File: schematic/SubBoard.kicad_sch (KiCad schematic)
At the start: 0 parts

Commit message: Progress on KiCAD schematics
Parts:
- added DS1: LCM SLOT, Display:WC1602A, symbol Display_Character:WC1602A
- added J2: LCM SLOT CONNECTOR, symbol Connector_Generic:Conn_02x11_Odd_Even
- added SD1: SD CARD SLOT, symbol Connector:Micro_SD_Card_Det2
- added SD2: SD CARD SLOT CONNECTOR, symbol Connector_Generic:Conn_02x08_Odd_Even
- added SW1: UP, Button_Switch_THT:SW_PUSH_6mm, symbol PCM_SL_Devices:Push_Button
- added SW2: DOWN, Button_Switch_THT:SW_PUSH_6mm, symbol PCM_SL_Devices:Push_Button
- added SW3: RIGHT, Button_Switch_THT:SW_PUSH_6mm, symbol PCM_SL_Devices:Push_Button
- added SW4: LEFT, Button_Switch_THT:SW_PUSH_6mm, symbol PCM_SL_Devices:Push_Button
- added SW5: ENTER, Button_Switch_THT:SW_PUSH_6mm, symbol PCM_SL_Devices:Push_Button
- added SW6: ESCAPE, Button_Switch_THT:SW_PUSH_6mm, symbol PCM_SL_Devices:Push_Button
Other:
- title: (none) -> Da Vinci Jr. 1.0 Sub Board schematic

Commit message: Update sub-board schematic
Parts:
- added Q2: FMBT3904W, Package_TO_SOT_SMD:SOT-323_SC-70, symbol Transistor_BJT:2SC4213
- added R1, R11, R21, R23, R25, R8: 100k, Resistor_THT:R_Axial_DIN0207_L6.3mm_D2.5mm_P10.16mm_Horizontal, symbol PCM_SL_Resistors:100k
- added R29: 2ohm, Resistor_THT:R_Axial_DIN0207_L6.3mm_D2.5mm_P10.16mm_Horizontal, symbol PCM_SL_Resistors:2ohm
- added R3, R30: 1k, Resistor_THT:R_Axial_DIN0207_L6.3mm_D2.5mm_P10.16mm_Horizontal, symbol PCM_SL_Resistors:1k
- added R5: 10k, Resistor_THT:R_Axial_DIN0207_L6.3mm_D2.5mm_P10.16mm_Horizontal, symbol PCM_SL_Resistors:10k
- added U1, U2: TXB0108PW, Package_SO:TSSOP-20_4.4x6.5mm_P0.65mm, symbol Logic_LevelTranslator:TXB0108PW
- renumbered DS1 to J3
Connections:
- net at SD1.1 (DAT2): now also SD2.16 (Pin_16)
- net at SD1.2 (DAT3/CD): now also SD2.14 (Pin_14)
- net at SD1.3 (CMD): now also SD2.12 (Pin_12)
- net at SD1.4 (VDD): now also SD2.9 (Pin_9)
- net at SD1.5 (CLK): now also SD2.7 (Pin_7)
- net GNDREF: now reaches SD1.6 (VSS)
- net GNDREF: now also J2.2 (Pin_2), J2.21 (Pin_21), J3.1 (VSS), SD1.SH (SHIELD), SD2.11 (Pin_11), SD2.13 (Pin_13), SD2.15 (Pin_15), SD2.2 (Pin_2), SD2.4 (Pin_4), SD2.6 (Pin_6), SW1.1, SW2.2, SW3.2, SW4.2, SW5.2, SW6.2, Q2.2 (E), R3.1
- net at SD1.7 (DAT0): now also SD2.5 (Pin_5)
- net at SD1.8 (DAT1): now also SD2.3 (Pin_3)
- net at SD1.9 (DET_B): now also SD2.10 (Pin_10)
- net at SW6.1: now also J2.15 (Pin_15), R25.1
- net at SW2.1: now also J2.16 (Pin_16), R8.1
- net at SW3.1: now also J2.19 (Pin_19), R11.1
- net at SW1.2: now also J2.18 (Pin_18), R1.1
- net at SW4.1: now also J2.17 (Pin_17), R21.1
- net at J2.1 (Pin_1): now also J3.2 (VDD), R29.2, R5.1, U1.19 (V_{CCB})
- net at J2.14 (Pin_14): now also R30.1
- net at J2.20 (Pin_20): now also SW5.1, R23.1
- net +5V: now reaches J2.22 (Pin_22)
- net +5V: now also R1.2, R11.2, R21.2, R23.2, R25.2, R8.2
- net at J3.15 (LED(+)): now also R29.1
- net at J3.16 (LED(-)): now also Q2.3 (C)
- net at J3.3 (VO): now also R3.2, R5.2
- new net: Q2.1 (B), R30.2
- no-connect marks 0 -> 3
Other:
- moved on the sheet: SW1, SW2

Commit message: Complete SubBoard schematic tracing
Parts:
- added R2, R28: 1k, Resistor_THT:R_Axial_DIN0207_L6.3mm_D2.5mm_P10.16mm_Horizontal, symbol PCM_SL_Resistors:1k
- R29: value 2ohm -> 2.7ohm
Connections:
- net GNDREF: now also U1.11 (GND), U2.11 (GND)
- net at J2.1 (Pin_1), J3.2 (VDD), R29.2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: now also U2.19 (V_{CCB})
- net +3.3V: now reaches SD1.4 (VDD), SD2.9 (Pin_9)
- net +3.3V: now also U1.2 (V_{CCA}), U2.2 (V_{CCA}), R2.2, R28.2
- net at U1.10 (OE): now also J3.14 (D7), U2.10 (OE), U2.12 (B8), R2.1, R28.1
- net at U1.15 (B5): now also J3.4 (RS)
- net at U1.16 (B4): now also J3.5 (R/W)
- net at U1.17 (B3): now also J3.6 (E)
- net at U1.4 (A3): now also J2.3 (Pin_3)
- net at U1.5 (A4): now also J2.4 (Pin_4)
- net at U1.6 (A5): now also J2.5 (Pin_5)
- net at J2.10 (Pin_10): now also U2.6 (A5)
- net at J2.11 (Pin_11): now also U2.7 (A6)
- net at J2.12 (Pin_12): now also U2.8 (A7)
- net at J2.13 (Pin_13): now also U2.9 (A8)
- net at J2.6 (Pin_6): now also U2.1 (A1)
- net at J2.7 (Pin_7): now also U2.3 (A2)
- net at J2.8 (Pin_8): now also U2.4 (A3)
- net at J2.9 (Pin_9): now also U2.5 (A4)
- net at J3.10 (D3): now also U2.16 (B4)
- net at J3.11 (D4): now also U2.15 (B5)
- net at J3.12 (D5): now also U2.14 (B6)
- net at J3.13 (D6): now also U2.13 (B7)
- net at J3.7 (D0): now also U2.20 (B1)
- net at J3.8 (D1): now also U2.18 (B2)
- net at J3.9 (D2): now also U2.17 (B3)
- no-connect marks 3 -> 13
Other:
- moved on the sheet: U2

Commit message: Update board schematics
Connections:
- net +3.3V: now also SD1.5 (VDD); no longer SD1.4 (VDD)
- net GNDREF: now also SD1.4 (VSS1), SD1.7 (VSS2); no longer SD1.6 (VSS)
- net at SD2.7 (Pin_7): now also SD1.6 (CLK); no longer SD1.5 (CLK)
- net at SD2.5 (Pin_5): now also SD1.8 (DAT0); no longer SD1.7 (DAT0)
- net at SD2.3 (Pin_3): now also SD1.9 (DAT1); no longer SD1.8 (DAT1)
- net at SD2.10 (Pin_10): now also SD1.11 (CD); no longer SD1.9 (DET_B)
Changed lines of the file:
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@@
 		(comment 1 "KEY/LCM/SD")
 	)
-	(text_box "DET_A is WP (Write Protect), DET_B is CD (Card Detect)"
-		(exclude_from_sim no)
-		(at 135.89 38.1 0)
-		(size 16.51 15.24)
-		(margins 0.9525 0.9525 0.9525 0.9525)
-		(stroke
-			(width 0)
-			(type solid)
-		)
-		(fill
-			(type none)
-		)
-		(effects
-			(font
-				(size 1.27 1.27)
-			)
-			(justify left top)
-		)
-	)
 	(junction
 		(at 232.41 153.67)
@@
 	)
 	(junction
+		(at 148.59 80.01)
+		(diameter 0)
+		(color 0 0 0 0)
+	)
+	(junction
 		(at 246.38 121.92)
 		(diameter 0)
@@
 	(wire
 		(pts
-			(xy 148.59 74.93) (xy 148.59 111.76)
+			(xy 151.13 74.93) (xy 151.13 111.76)
 		)
 		(stroke
@@
 	(wire
 		(pts
+			(xy 148.59 80.01) (xy 163.83 80.01)
+		)
+		(stroke
+			(width 0)
+			(type default)
+		)
+	)
+	(wire
+		(pts
 			(xy 83.82 74.93) (xy 83.82 76.2)
 		)
@@
 	(wire
 		(pts
-			(xy 151.13 114.3) (xy 234.95 114.3)
+			(xy 153.67 114.3) (xy 234.95 114.3)
 		)
 		(stroke
@@
 	(wire
 		(pts
-			(xy 140.97 80.01) (xy 163.83 80.01)
+			(xy 140.97 80.01) (xy 148.59 80.01)
 		)
 		(stroke
@@
 	(wire
 		(pts
-			(xy 151.13 74.93) (xy 151.13 114.3)
+			(xy 153.67 74.93) (xy 153.67 114.3)
 		)
 		(stroke
@@
 	(wire
 		(pts
-			(xy 148.59 111.76) (xy 232.41 111.76)
+			(xy 151.13 111.76) (xy 232.41 111.76)
 		)
 		(stroke
@@
 	(wire
 		(pts
-			(xy 153.67 74.93) (xy 153.67 116.84)
+			(xy 156.21 74.93) (xy 156.21 116.84)
 		)
 		(stroke
@@
 	(wire
 		(pts
-			(xy 153.67 116.84) (xy 237.49 116.84)
+			(xy 156.21 116.84) (xy 237.49 116.84)
 		)
 		(stroke
@@
 	(wire
 		(pts
+			(xy 148.59 74.93) (xy 148.59 80.01)
+		)
+		(stroke
+			(width 0)
+			(type default)
+		)
+	)
+	(wire
+		(pts
 			(xy 209.55 129.54) (xy 215.9 129.54)
 		)
@@
 	(wire
 		(pts
-			(xy 130.81 31.75) (xy 130.81 27.94)
+			(xy 132.08 31.75) (xy 132.08 27.94)
 		)
 		(stroke
@@
 	(wire
 		(pts
-			(xy 130.81 27.94) (xy 123.19 27.94)
+			(xy 132.08 27.94) (xy 123.19 27.94)
 		)
 		(stroke
@@
 	(symbol
 		(lib_id "Connector:Micro_SD_Card_Det2")
-		(at 143.51 52.07 270)
+		(at 144.78 52.07 270)
 		(mirror x)
 		(unit 1)
@@
 		(dnp no)
 		(property "Reference" "SD1"
-			(at 125.73 50.1649 90)
+			(at 127 50.1649 90)
 			(show_name no)
 			(do_not_autoplace no)
@@
 		)
 		(property "Value" "SD CARD SLOT"
-			(at 125.73 52.7049 90)
+			(at 127 52.7049 90)
 			(show_name no)
 			(do_not_autoplace no)
@@
 		)
 		(property "Footprint" ""
-			(at 161.29 0 0)
+			(at 162.56 0 0)
 			(hide yes)
 			(show_name no)
@@
 		)
 		(property "Datasheet" "https://www.hirose.com/en/product/document?clcode=&productname=&series=DM3&documenttype=Catalog&lang=en&documentid=D49662_en"
-			(at 146.05 49.53 0)
+			(at 147.32 49.53 0)
 			(hide yes)
 			(show_name no)
@@
 		)
 		(property "Description" "Micro SD Card Socket with two card detection pins"
-			(at 143.51 52.07 0)
+			(at 144.78 52.07 0)
 			(hide yes)
 			(show_name no)
@@
 		(pin "10"
 		)
+		(pin "11"
+		)
 		(instances

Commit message: Organize hardware documentation and pinouts
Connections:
- net +3.3V: now also SD2.8 (Pin_8)
- no-connect marks 13 -> 12
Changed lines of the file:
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@@
+		(color 0 0 0 0)
+	)
+	(junction
+		(at 213.36 156.21)
+		(diameter 0)
 		(color 0 0 0 0)
 	)
@@
 	)
 	(no_connect
-		(at 227.33 138.43)
-	)
-	(no_connect
 		(at 52.07 111.76)
 	)
@@
 	(wire
 		(pts
+			(xy 227.33 138.43) (xy 227.33 137.16)
+		)
+		(stroke
+			(width 0)
+			(type default)
+		)
+	)
+	(wire
+		(pts
 			(xy 52.07 104.14) (xy 67.31 104.14)
 		)
@@
 	(wire
 		(pts
+			(xy 213.36 137.16) (xy 213.36 156.21)
+		)
+		(stroke
+			(width 0)
+			(type default)
+		)
+	)
+	(wire
+		(pts
 			(xy 90.17 137.16) (xy 90.17 142.24)
 		)
@@
 	(wire
 		(pts
-			(xy 229.87 156.21) (xy 146.05 156.21)
+			(xy 229.87 156.21) (xy 213.36 156.21)
 		)
 		(stroke
@@
 	(wire
 		(pts
+			(xy 227.33 137.16) (xy 213.36 137.16)
+		)
+		(stroke
+			(width 0)
+			(type default)
+		)
+	)
+	(wire
+		(pts
 			(xy 132.08 27.94) (xy 123.19 27.94)
 		)
@@
 		)
 		(stroke
+			(width 0)
+			(type default)
+		)
+	)
+	(wire
+		(pts
+			(xy 213.36 156.21) (xy 146.05 156.21)
+		)
+		(stroke

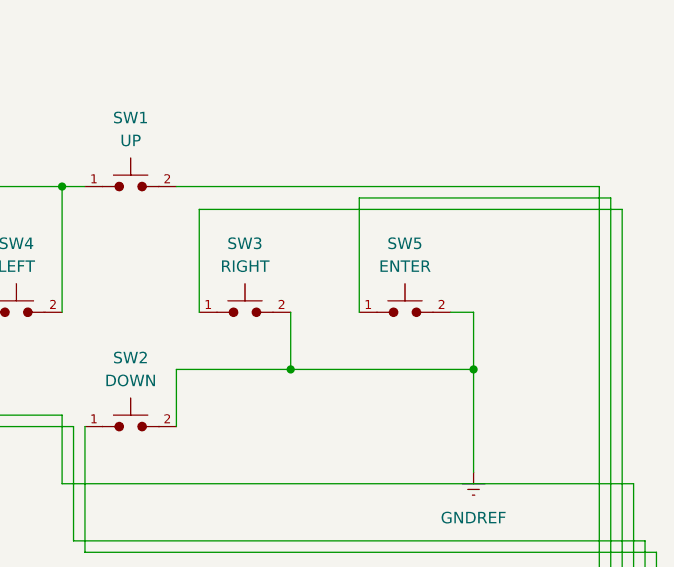
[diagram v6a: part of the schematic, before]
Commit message: Updata TODO and schematics
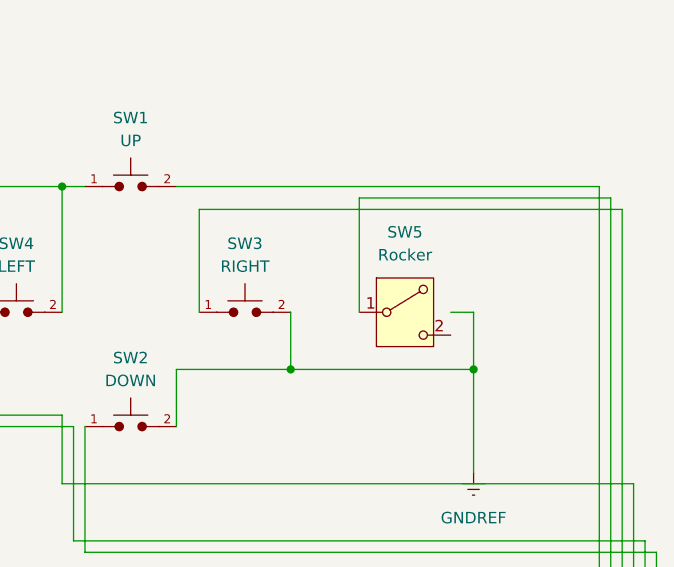
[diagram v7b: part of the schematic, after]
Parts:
- SW5: value ENTER -> Rocker; footprint Button_Switch_THT:SW_PUSH_6mm -> (none)
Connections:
- net GNDREF: no longer SW5.2
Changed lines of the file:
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@@
 	)
 	(symbol
+		(lib_name "Push_Button_1")
 		(lib_id "PCM_SL_Devices:Push_Button")
 		(at 252.73 72.39 0)
@@
 		(fields_autoplaced yes)
 		(property "Reference" "SW5"
-			(at 252.73 64.77 0)
+			(at 252.73 63.5 0)
 			(show_name no)
 			(do_not_autoplace no)
@@
 			)
 		)
-		(property "Value" "ENTER"
-			(at 252.73 67.31 0)
+		(property "Value" "Rocker"
+			(at 252.73 66.04 0)
 			(show_name no)
 			(do_not_autoplace no)
@@
 			)
 		)
-		(property "Footprint" "Button_Switch_THT:SW_PUSH_6mm"
-			(at 252.603 75.565 0)
+		(property "Footprint" ""
+			(at 252.73 72.39 0)
 			(hide yes)
 			(show_name no)
@@
 		)
 		(property "Datasheet" ""
-			(at 252.73 72.39 0)
+			(at 252.73 80.01 0)
 			(hide yes)
 			(show_name no)
@@
 			)
 		)
-		(property "Description" "Common 6mmx6mm Push Button"
+		(property "Description" "Switch, single pole double throw"
 			(at 252.73 72.39 0)
 			(hide yes)
@@
 					(reference "SW5")
 					(unit 1)
+				)
+				(path "/1e12c736-bef9-40e8-b505-1000ff77a2bb/d610c2e8-63cd-4e0f-98e2-bf1a99df609b"
+					(reference "SW5")
+					(unit 1)

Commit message: Fix the broken button
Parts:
- SW5: value Rocker -> ENTER; footprint (none) -> Button_Switch_THT:SW_PUSH_6mm
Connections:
- net GNDREF: now also SW5.2
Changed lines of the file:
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@@
+	)
+	(symbol
+		(lib_id "PCM_SL_Devices:Push_Button")
+		(at 252.73 72.39 0)
+		(unit 1)
+		(body_style 1)
+		(exclude_from_sim no)
+		(in_bom yes)
+		(on_board yes)
+		(in_pos_files yes)
+		(dnp no)
+		(fields_autoplaced yes)
+		(property "Reference" "SW5"
+			(at 252.73 64.77 0)
+			(show_name no)
+			(do_not_autoplace no)
+			(effects
+				(font
+					(size 1.27 1.27)
+				)
+			)
+		)
+		(property "Value" "ENTER"
+			(at 252.73 67.31 0)
+			(show_name no)
+			(do_not_autoplace no)
+			(effects
+				(font
+					(size 1.27 1.27)
+				)
+			)
+		)
+		(property "Footprint" "Button_Switch_THT:SW_PUSH_6mm"
+			(at 252.603 75.565 0)
+			(hide yes)
+			(show_name no)
+			(do_not_autoplace no)
+			(effects
+				(font
+					(size 1.27 1.27)
+				)
+			)
+		)
+		(property "Datasheet" ""
+			(at 252.73 72.39 0)
+			(hide yes)
+			(show_name no)
+			(do_not_autoplace no)
+			(effects
+				(font
+					(size 1.27 1.27)
+				)
+			)
+		)
+		(property "Description" "Common 6mmx6mm Push Button"
+			(at 252.73 72.39 0)
+			(hide yes)
+			(show_name no)
+			(do_not_autoplace no)
+			(effects
+				(font
+					(size 1.27 1.27)
+				)
+			)
+		)
+		(pin "2"
+		)
+		(pin "1"
+		)
+		(instances
+			(project "DaVinciJr1.0"
+				(path "/1e12c736-bef9-40e8-b505-1000ff77a2bb/b418c2e6-1ad3-4591-9cff-9544514ed08e"
+					(reference "SW5")
+					(unit 1)
+				)
+			)
+		)
 	)
 	(symbol
@@
 					(unit 1)
 				)
-			)
-		)
-	)
-	(symbol
-		(lib_name "Push_Button_1")
-		(lib_id "PCM_SL_Devices:Push_Button")
-		(at 252.73 72.39 0)
-		(unit 1)
-		(body_style 1)
-		(exclude_from_sim no)
-		(in_bom yes)
-		(on_board yes)
-		(in_pos_files yes)
-		(dnp no)
-		(fields_autoplaced yes)
-		(property "Reference" "SW5"
-			(at 252.73 63.5 0)
-			(show_name no)
-			(do_not_autoplace no)
-			(effects
-				(font
-					(size 1.27 1.27)
-				)
-			)
-		)
-		(property "Value" "Rocker"
-			(at 252.73 66.04 0)
-			(show_name no)
-			(do_not_autoplace no)
-			(effects
-				(font
-					(size 1.27 1.27)
-				)
-			)
-		)
-		(property "Footprint" ""
-			(at 252.73 72.39 0)
-			(hide yes)
-			(show_name no)
-			(do_not_autoplace no)
-			(effects
-				(font
-					(size 1.27 1.27)
-				)
-			)
-		)
-		(property "Datasheet" ""
-			(at 252.73 80.01 0)
-			(hide yes)
-			(show_name no)
-			(do_not_autoplace no)
-			(effects
-				(font
-					(size 1.27 1.27)
-				)
-			)
-		)
-		(property "Description" "Switch, single pole double throw"
-			(at 252.73 72.39 0)
-			(hide yes)
-			(show_name no)
-			(do_not_autoplace no)
-			(effects
-				(font
-					(size 1.27 1.27)
-				)
-			)
-		)
-		(pin "2"
-		)
-		(pin "1"
-		)
-		(instances
-			(project "DaVinciJr1.0"
-				(path "/1e12c736-bef9-40e8-b505-1000ff77a2bb/b418c2e6-1ad3-4591-9cff-9544514ed08e"
-					(reference "SW5")
-					(unit 1)
-				)
-				(path "/1e12c736-bef9-40e8-b505-1000ff77a2bb/d610c2e8-63cd-4e0f-98e2-bf1a99df609b"
-					(reference "SW5")
-					(unit 1)
-				)
